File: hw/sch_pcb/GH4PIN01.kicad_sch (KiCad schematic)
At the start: 7 parts, among them J1 SM04B-GHS-TB, J2 SM04B-GHS-TB, J3 HEADER_2x05_PARALLEL, M1 HOLE M3, M2 HOLE M3, M3 HOLE, M4 HOLE

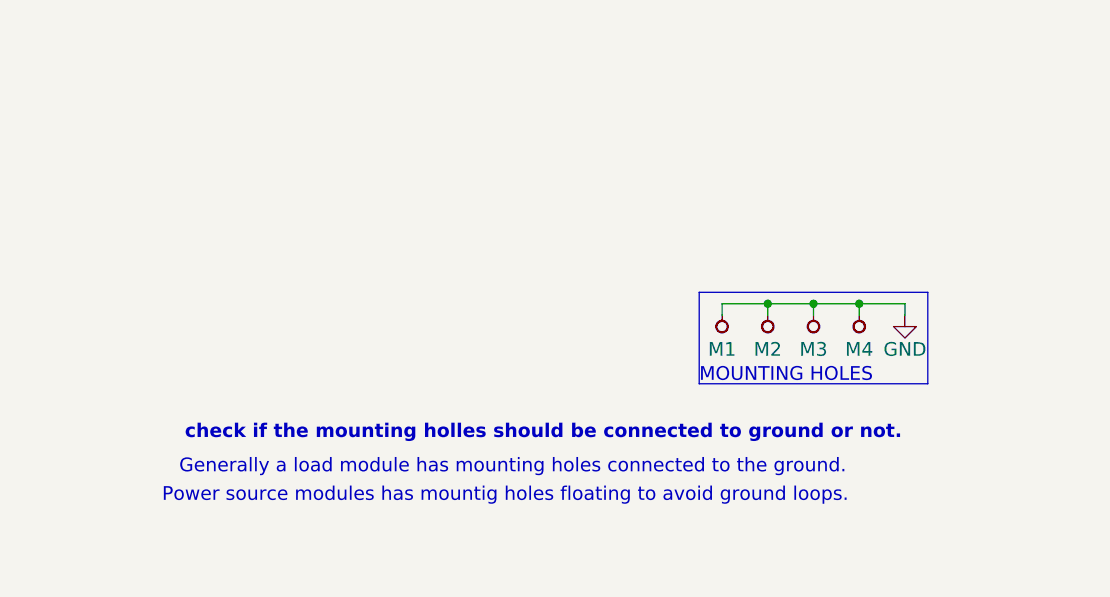
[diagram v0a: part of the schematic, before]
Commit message: Cleanup and save in KiCAD 7.
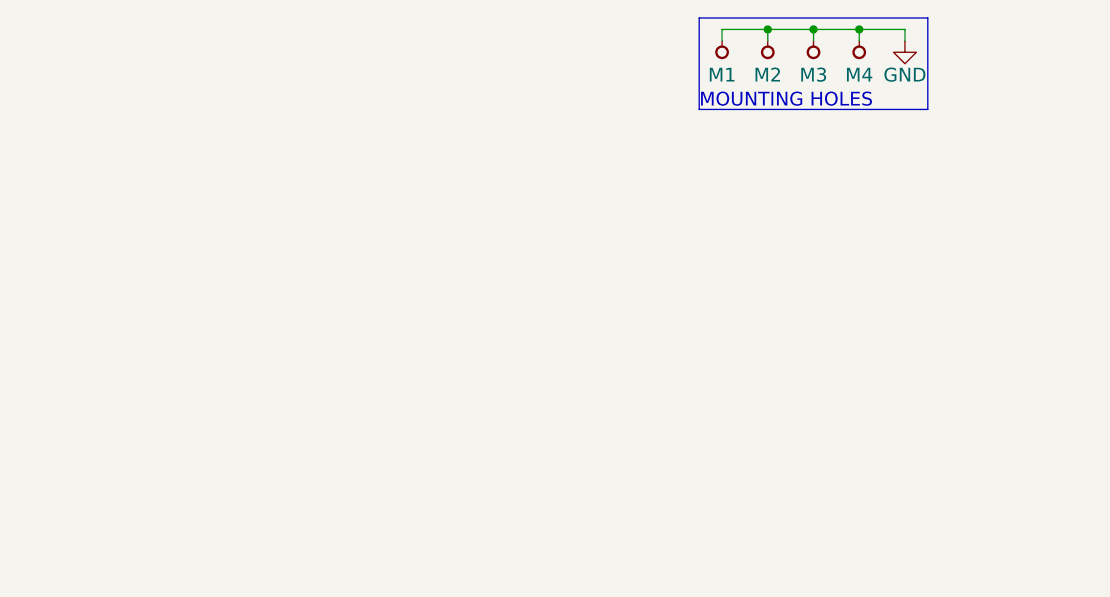
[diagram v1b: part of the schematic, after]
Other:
- note removed: "Generally a load module has mounting holes connected to the ground."
- note removed: "Power source modules has mountig holes floating to avoid ground loops."
- note removed: "check if the mounting holles should be connected to ground or not."
- moved on the sheet: M1, M2, M3, M4

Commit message: The routed layout.
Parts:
- added J4, J5: SM04B-GHS-TB, Connector_JST:JST_GH_SM04B-GHS-TB_1x04-1MP_P1.25mm_Horizontal, symbol MLAB_CONNECTORS_JST:SM04B-GHS-TB
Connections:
- net GND: now also J4.4, J4.MP, J5.4, J5.MP
- net +5V: now reaches J1.1, J2.1, J3.5, J3.6
- net +5V: now also J4.1, J5.1
- net SCL: now reaches J1.2, J2.2, J3.3, J3.4
- net SCL: now also J4.2, J5.2
- net SDA: now reaches J1.3, J2.3, J3.7, J3.8
- net SDA: now also J4.3, J5.3
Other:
- moved on the sheet: J1, J2, J3

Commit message: Improve manufacturing texts.
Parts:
- added FID1, FID2: Fiducial, Fiducial:Fiducial_1mm_Mask2mm, symbol Mechanical:Fiducial
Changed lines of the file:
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@@
+    )
+  )
+  (symbol (lib_id "Mechanical:Fiducial") (at 259.08 45.085 0) (unit 1)
+    (in_bom yes) (on_board yes) (dnp no) (fields_autoplaced)
+    (property "Reference" "FID1" (at 261.239 43.8729 0)
+      (effects (font (size 1.27 1.27)) (justify left))
+    )
+    (property "Value" "Fiducial" (at 261.239 46.2971 0)
+      (effects (font (size 1.27 1.27)) (justify left))
+    )
+    (property "Footprint" "Fiducial:Fiducial_1mm_Mask2mm" (at 259.08 45.085 0)
+      (effects (font (size 1.27 1.27)) hide)
+    )
+    (property "Datasheet" "~" (at 259.08 45.085 0)
+      (effects (font (size 1.27 1.27)) hide)
+    )
+    (instances
+      (project "GH4PIN01"
+        (path "/2ae32537-a16f-4c5b-a56b-c6dddfb8ddb4"
+          (reference "FID1") (unit 1)
+        )
+      )
     )
   )
@@
         )
       )
+    )
+  )
+  (symbol (lib_id "Mechanical:Fiducial") (at 259.08 56.515 0) (unit 1)
+    (in_bom yes) (on_board yes) (dnp no) (fields_autoplaced)
+    (property "Reference" "FID2" (at 261.239 55.3029 0)
+      (effects (font (size 1.27 1.27)) (justify left))
+    )
+    (property "Value" "Fiducial" (at 261.239 57.7271 0)
+      (effects (font (size 1.27 1.27)) (justify left))
+    )
+    (property "Footprint" "Fiducial:Fiducial_1mm_Mask2mm" (at 259.08 56.515 0)
+      (effects (font (size 1.27 1.27)) hide)
+    )
+    (property "Datasheet" "~" (at 259.08 56.515 0)
+      (effects (font (size 1.27 1.27)) hide)
+    )
+    (instances
+      (project "GH4PIN01"
+        (path "/2ae32537-a16f-4c5b-a56b-c6dddfb8ddb4"
+          (reference "FID2") (unit 1)
+        )
+      )

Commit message: Add labels for CAN bus.
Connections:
- net SCL renamed SCL/CAN_H
- net SDA renamed SDA/CAN_L
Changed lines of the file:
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@@
     (rev "A")
     (company "Mlab www.mlab.cz")
-    (comment 1 "PixHawk I2C - MLAB interface")
+    (comment 1 "PixHawk I2C or CAN - MLAB interface")
     (comment 2 "Alsa-Tucnak")
   )
@@
     (stroke (width 0) (type default))
   )
-  (wire (pts (xy 151.765 61.595) (xy 160.655 61.595))
+  (wire (pts (xy 144.78 61.595) (xy 160.655 61.595))
     (stroke (width 0) (type default))
   )
@@
     (stroke (width 0) (type default))
   )
-  (wire (pts (xy 151.765 64.135) (xy 160.655 64.135))
+  (wire (pts (xy 144.78 64.135) (xy 160.655 64.135))
     (stroke (width 0) (type default))
   )
@@
     (stroke (width 0) (type default))
   )
-  (wire (pts (xy 121.285 61.595) (xy 112.395 61.595))
+  (wire (pts (xy 112.395 61.595) (xy 128.27 61.595))
     (stroke (width 0) (type default))
   )
@@
     (stroke (width 0) (type default))
   )
-  (wire (pts (xy 151.765 59.055) (xy 160.655 59.055))
+  (wire (pts (xy 145.415 59.055) (xy 160.655 59.055))
     (stroke (width 0) (type default))
   )
@@
     (stroke (width 0) (type default))
   )
-  (wire (pts (xy 121.285 64.135) (xy 112.395 64.135))
+  (wire (pts (xy 112.395 64.135) (xy 128.27 64.135))
     (stroke (width 0) (type default))
   )
@@
     (effects (font (size 1.524 1.524)) (justify left bottom))
   )
-  (label "SDA" (at 151.765 64.135 0) (fields_autoplaced)
-    (effects (font (size 1.524 1.524)) (justify left bottom))
-  )
-  (label "SDA" (at 121.285 64.135 180) (fields_autoplaced)
+  (label "SDA{slash}CAN_L" (at 144.78 64.135 0) (fields_autoplaced)
+    (effects (font (size 1.524 1.524)) (justify left bottom))
+  )
+  (label "SDA{slash}CAN_L" (at 128.27 64.135 180) (fields_autoplaced)
     (effects (font (size 1.524 1.524)) (justify right bottom))
   )
-  (label "SCL" (at 116.205 84.455 0) (fields_autoplaced)
-    (effects (font (size 1.524 1.524)) (justify left bottom))
-  )
-  (label "SDA" (at 148.59 86.995 0) (fields_autoplaced)
-    (effects (font (size 1.524 1.524)) (justify left bottom))
-  )
-  (label "+5V" (at 151.765 59.055 0) (fields_autoplaced)
+  (label "SCL{slash}CAN_H" (at 116.205 84.455 0) (fields_autoplaced)
+    (effects (font (size 1.524 1.524)) (justify left bottom))
+  )
+  (label "SDA{slash}CAN_L" (at 141.605 86.995 0) (fields_autoplaced)
+    (effects (font (size 1.524 1.524)) (justify left bottom))
+  )
+  (label "+5V" (at 145.415 59.055 0) (fields_autoplaced)
     (effects (font (size 1.524 1.524)) (justify left bottom))
   )
@@
     (effects (font (size 1.524 1.524)) (justify left bottom))
   )
-  (label "SCL" (at 121.285 61.595 180) (fields_autoplaced)
+  (label "SCL{slash}CAN_H" (at 128.27 61.595 180) (fields_autoplaced)
     (effects (font (size 1.524 1.524)) (justify right bottom))
   )
-  (label "SCL" (at 151.765 61.595 0) (fields_autoplaced)
-    (effects (font (size 1.524 1.524)) (justify left bottom))
-  )
+  (label "SCL{slash}CAN_H" (at 144.78 61.595 0) (fields_autoplaced)
+    (effects (font (size 1.524 1.524)) (justify left bottom))
+  )
